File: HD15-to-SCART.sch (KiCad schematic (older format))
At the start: 3 parts

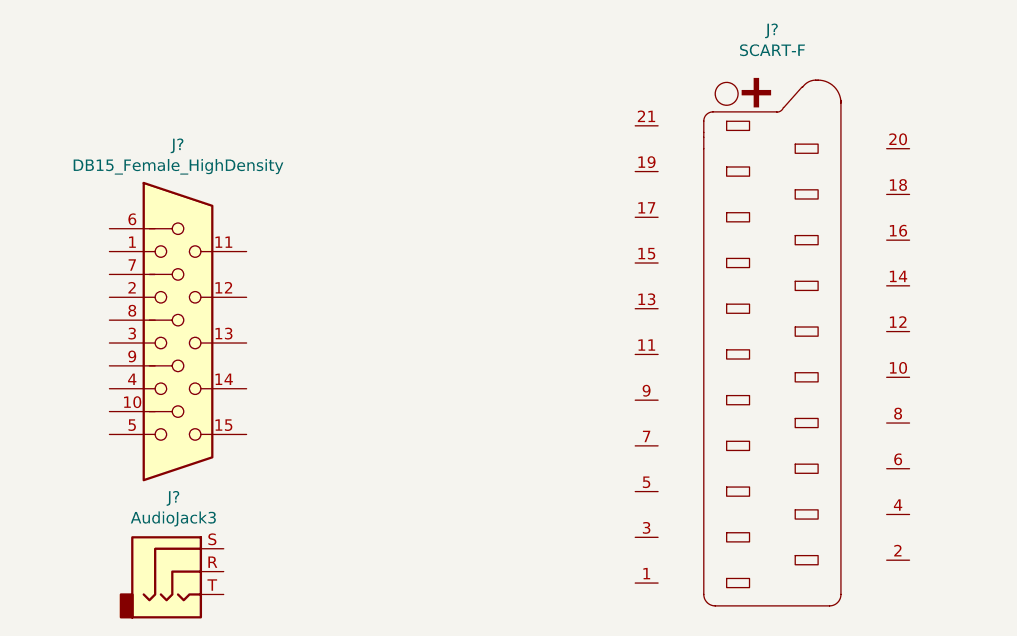
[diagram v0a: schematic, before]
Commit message: Finished schematic and designed pcb
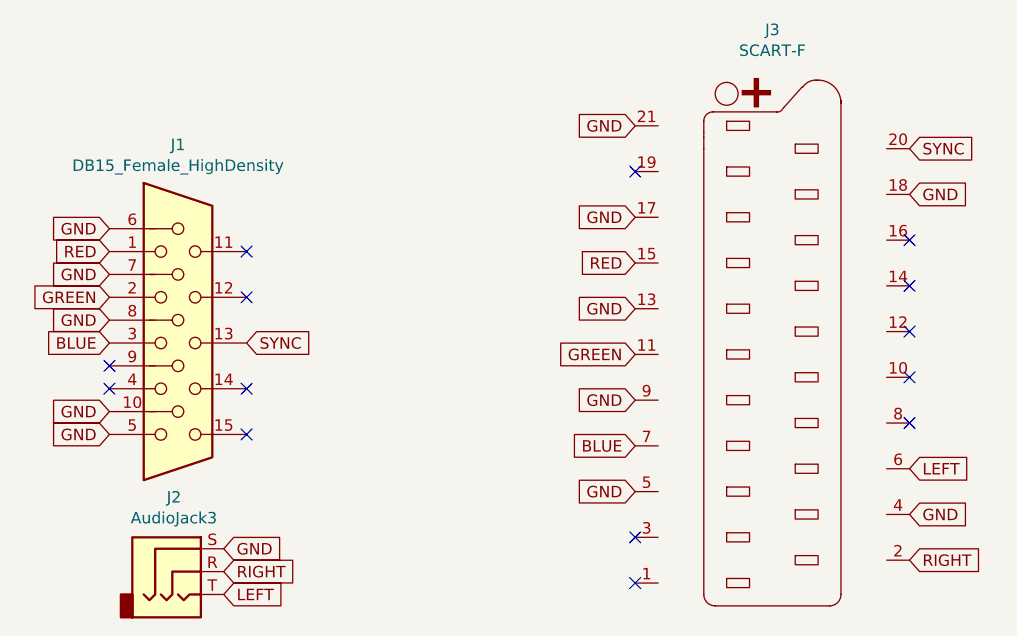
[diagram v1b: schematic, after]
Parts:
- J1: renamed from J?; footprint (none) -> Tinkerplunk:VGA
- J2: renamed from J?; footprint (none) -> Tinkerplunk:Tall_Skinny_Headphone_Universal_CUI_SJ1-353XNX
- J3: renamed from J?; footprint (none) -> Tinkerplunk:MALE_SCART
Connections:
- net GREEN: now reaches J3.11 (P11)
- net GREEN: now also J1.2
- net GND: now reaches J3.13 (P13)
- net GND: now also J1.10, J1.5, J1.6, J1.7, J1.8, J2.S, J3.17 (P17), J3.18 (P18), J3.21 (P21), J3.4 (P4), J3.5 (P5), J3.9 (P9)
- net RED: now reaches J3.15 (P15)
- net RED: now also J1.1
- net RIGHT: now reaches J3.2 (P2)
- net RIGHT: now also J2.R
- net SYNC: now reaches J3.20 (P20)
- net SYNC: now also J1.13
- net LEFT: now reaches J3.6 (P6)
- net LEFT: now also J2.T
- net BLUE: now reaches J3.7 (P7)
- net BLUE: now also J1.3
- no-connect marks 0 -> 14
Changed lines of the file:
@@
 EESchema Schematic File Version 4
+LIBS:HD15-to-SCART-cache
 EELAYER 29 0
 EELAYER END
@@
 $EndDescr
 $Comp
-L Connector:SCART-F J?
+L Connector:SCART-F J3
 U 1 1 5D012D32
 P 7400 3500
-F 0 "J?" H 7400 4920 50  0000 C CNN
+F 0 "J3" H 7400 4920 50  0000 C CNN
 F 1 "SCART-F" H 7400 4829 50  0000 C CNN
-F 2 "" H 7400 3550 50  0001 C CNN
+F 2 "Tinkerplunk:MALE_SCART" H 7400 3550 50  0001 C CNN
 F 3 " ~" H 7400 3550 50  0001 C CNN
 	1    7400 3500
@@
 $EndComp
 $Comp
-L Connector:DB15_Female_HighDensity J?
+L Connector:DB15_Female_HighDensity J1
 U 1 1 5D013D70
 P 4800 3450
-F 0 "J?" H 4800 4317 50  0000 C CNN
+F 0 "J1" H 4800 4317 50  0000 C CNN
 F 1 "DB15_Female_HighDensity" H 4800 4226 50  0000 C CNN
-F 2 "" H 3850 3850 50  0001 C CNN
+F 2 "Tinkerplunk:VGA" H 3850 3850 50  0001 C CNN
 F 3 " ~" H 3850 3850 50  0001 C CNN
 	1    4800 3450
@@
 $EndComp
 $Comp
-L Connector:AudioJack3 J?
+L Connector:AudioJack3 J2
 U 1 1 5D01540E
 P 4800 4450
-F 0 "J?" H 4782 4775 50  0000 C CNN
+F 0 "J2" H 4782 4775 50  0000 C CNN
 F 1 "AudioJack3" H 4782 4684 50  0000 C CNN
-F 2 "" H 4800 4450 50  0001 C CNN
+F 2 "Tinkerplunk:Tall_Skinny_Headphone_Universal_CUI_SJ1-353XNX" H 4800 4450 50  0001 C CNN
 F 3 "~" H 4800 4450 50  0001 C CNN
 	1    4800 4450
 	1    0    0    -1
 $EndComp
+Text GLabel 6800 2500 0    50   Input ~ 0
+GND
+Text GLabel 6800 2900 0    50   Input ~ 0
+GND
+Text GLabel 6800 3300 0    50   Input ~ 0
+GND
+Text GLabel 6800 3700 0    50   Input ~ 0
+GND
+Text GLabel 6800 4100 0    50   Input ~ 0
+GND
+Text GLabel 8000 4200 2    50   Input ~ 0
+GND
+Text GLabel 8000 2800 2    50   Input ~ 0
+GND
+Text GLabel 8000 4400 2    50   Input ~ 0
+RIGHT
+Text GLabel 8000 4000 2    50   Input ~ 0
+LEFT
+NoConn ~ 6800 4500
+NoConn ~ 6800 4300
+NoConn ~ 6800 2700
+NoConn ~ 8000 3000
+NoConn ~ 8000 3200
+NoConn ~ 8000 3400
+NoConn ~ 8000 3600
+NoConn ~ 8000 3800
+Text GLabel 6800 3100 0    50   Input ~ 0
+RED
+Text GLabel 6800 3500 0    50   Input ~ 0
+GREEN
+Text GLabel 6800 3900 0    50   Input ~ 0
+BLUE
+Text GLabel 8000 2600 2    50   Input ~ 0
+SYNC
+Text GLabel 4500 3050 0    50   Input ~ 0
+RED
+Text GLabel 4500 3250 0    50   Input ~ 0
+GREEN
+Text GLabel 4500 3450 0    50   Input ~ 0
+BLUE
+Text GLabel 5100 3450 2    50   Input ~ 0
+SYNC
+Text GLabel 5000 4350 2    50   Input ~ 0
+GND
+Text GLabel 5000 4550 2    50   Input ~ 0
+LEFT
+Text GLabel 5000 4450 2    50   Input ~ 0
+RIGHT
+Text GLabel 4500 3850 0    50   Input ~ 0
+GND
+Text GLabel 4500 2950 0    50   Input ~ 0
+GND
+Text GLabel 4500 3150 0    50   Input ~ 0
+GND
+Text GLabel 4500 3350 0    50   Input ~ 0
+GND
+Text GLabel 4500 3750 0    50   Input ~ 0
+GND
+NoConn ~ 4500 3550
+NoConn ~ 4500 3650
+NoConn ~ 5100 3050
+NoConn ~ 5100 3250
+NoConn ~ 5100 3650
+NoConn ~ 5100 3850
 $EndSCHEMATC
